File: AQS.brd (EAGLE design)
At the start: 70 x 60 mm, 44 parts, among them IC1 BME680, IC3 CP2102N-A01-GQFN24, IC4 ESPWROOM32, J1 ESP-PROG-2X3-1.27-SHROUDED, J2 M02X5-1.27-S, J3 USB-C-16P-16P, Q1 MMDT3904, Q2 2N7002

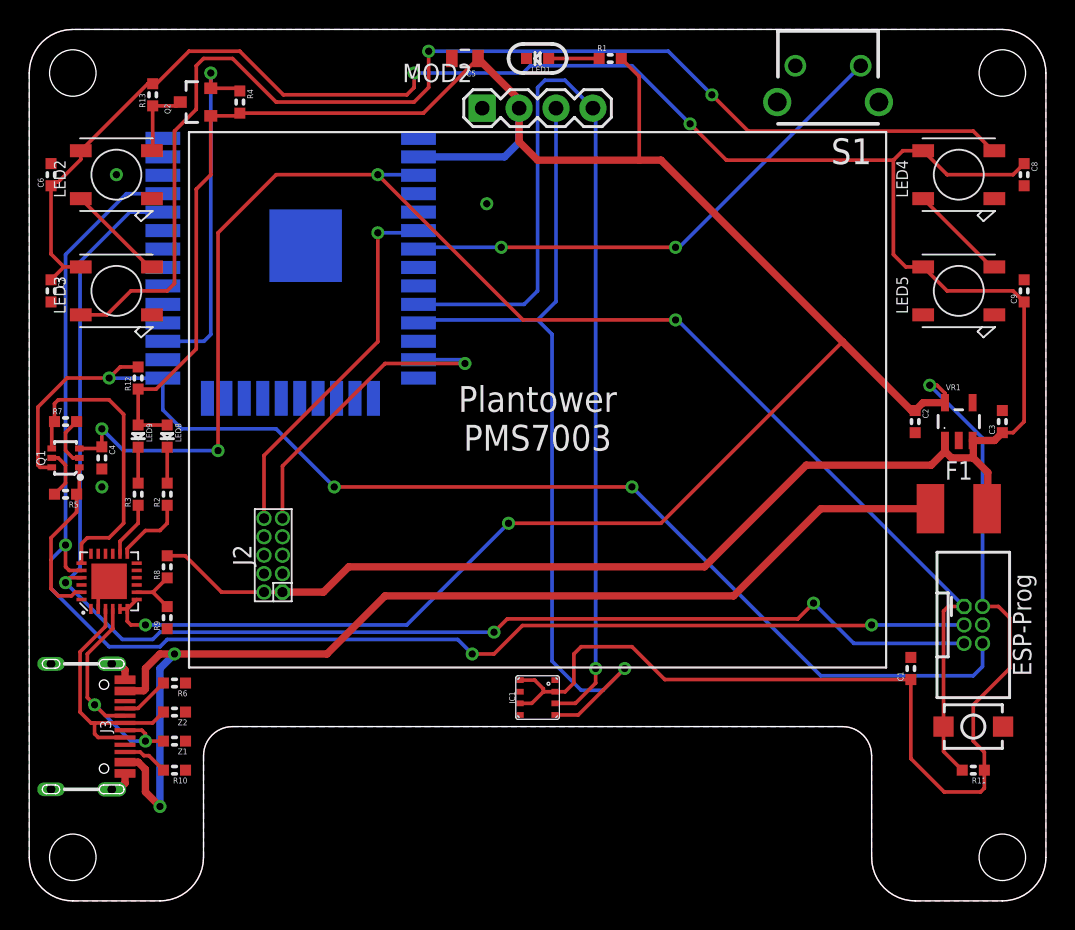
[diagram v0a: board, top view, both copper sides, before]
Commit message: Major update to use 240x240 SPI LCD
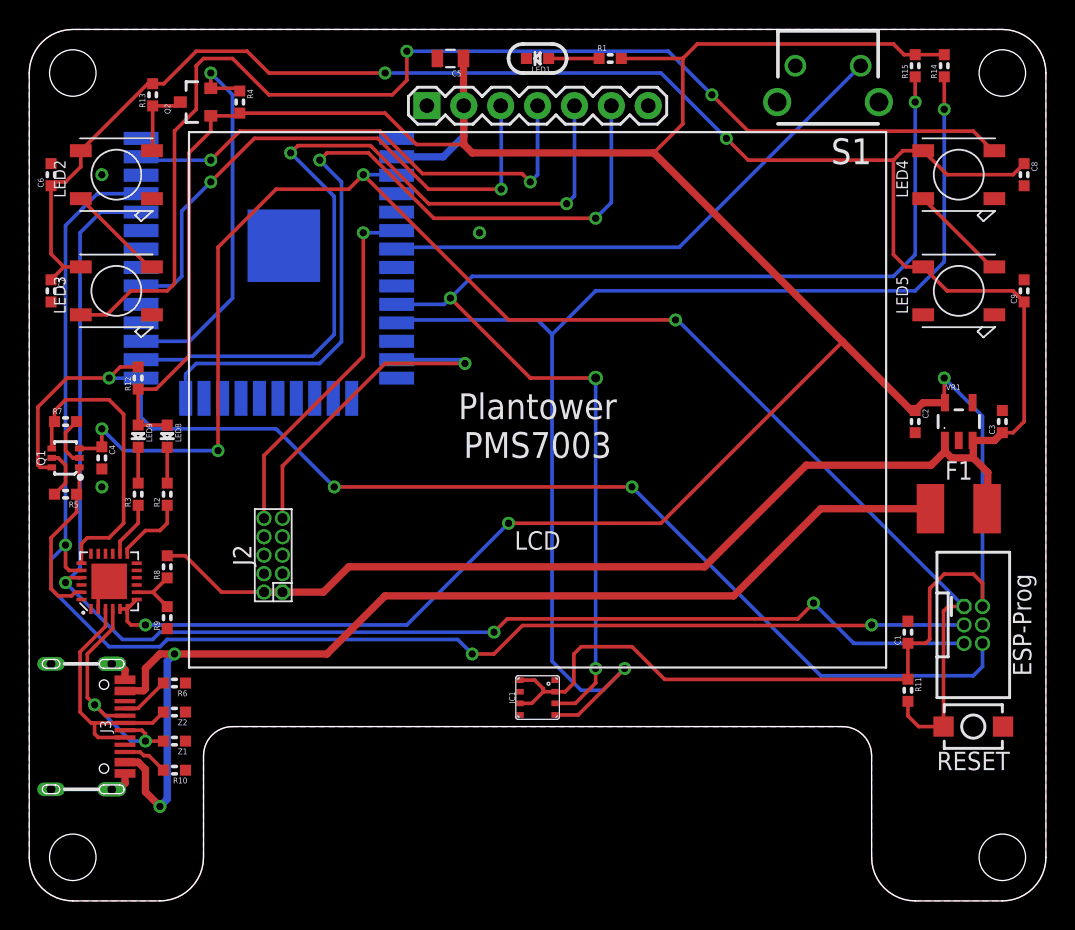
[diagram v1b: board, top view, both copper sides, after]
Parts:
- removed MOD2: OLED-I2C-128X64-0.96-HEADER, SuperHouse-Displays:OLED-128X64-0.96-HEADER
- added LCD: OLED-SPI-HEADER, SuperHouse-Displays:OLED-240X240-1.3-HEADER
- added R14, R15: 4K7, SuperHouse-DiscreteSemi:R0603
- moved R11 7.11 mm to (60.5, 15.5), turned to 270 degrees
- moved C1 2.51 mm to (60.5, 19.5)
- moved IC4 1.50 mm to (16.5, 55.0)
- moved C5 1.00 mm to (29.0, 59.0)
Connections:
- new net GPIO15: IC4.23
- new net GPIO18: IC4.30, LCD.SCK
- new net GPIO19: IC4.31
- new net GPIO2: IC4.24, LCD.DC
- new net GPIO23: IC4.37, LCD.SDA
- new net GPIO4: IC4.26, LCD.RES
- net 3.3V: now also LCD.VCC, R14.2, R15.2; no longer MOD2.VCC
- net GND: now also LCD.GND; no longer MOD2.GND
- net SCL: now also R14.1; no longer MOD2.SCL
- net SDA: now also R15.1; no longer MOD2.SDA
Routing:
- net GPIO2: track 0.00 -> 55.7 mm, vias 0 -> 2
- net GPIO4: track 0.00 -> 55.6 mm, vias 0 -> 2
- net GPIO18: track 0.00 -> 38.9 mm, vias 0 -> 2
- net GPIO23: track 0.00 -> 34.6 mm, vias 0 -> 2
- net SCL: track 59.9 -> 88.1 mm, vias 1 -> 2
- net SDA: track 70.4 -> 86.0 mm, vias 1 -> 4
- net 3.3V: track 246.6 -> 253.1 mm
- net GPIO16: track 24.6 -> 26.8 mm
- net 5V: track 182.0 -> 180.0 mm
- net PMS_SET: track 22.4 -> 23.9 mm
- net BUTTON: track 35.7 -> 37.2 mm, vias 2 -> 0
- net PMS_TX: track 25.8 -> 24.9 mm
- net !RESET: track 107.6 -> 106.8 mm
- net N$12: track 85.1 -> 84.4 mm
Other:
- board text added: "I2C Address: 0x77: BME680"
- board text added: "Pin Assignments: GPIO2: TFT_DC GPIO4: TFT_RST GPIO14: SET for PMS7003 GPIO15: TFT_CS GPIO16: WS2812B GPIO18: TFT_SCLK GPIO19: TFT_MISO GPIO23: TFT_MOSI GPIO25: SDA GPIO26: SCL GPIO34: Rx from PMS7003 Tx GPIO35: Button"
- board text added: "RESET"
- board text removed: "Pin Assignments: IO14: SET for PMS7003 IO16: WS2812B IO25: SDA IO26: SCL IO34: Rx from PMS7003 IO35: Button I2C Addresses: 0x3C: 128x64 OLED 0x77: BME280"

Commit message: Moved mode button to GPIO0
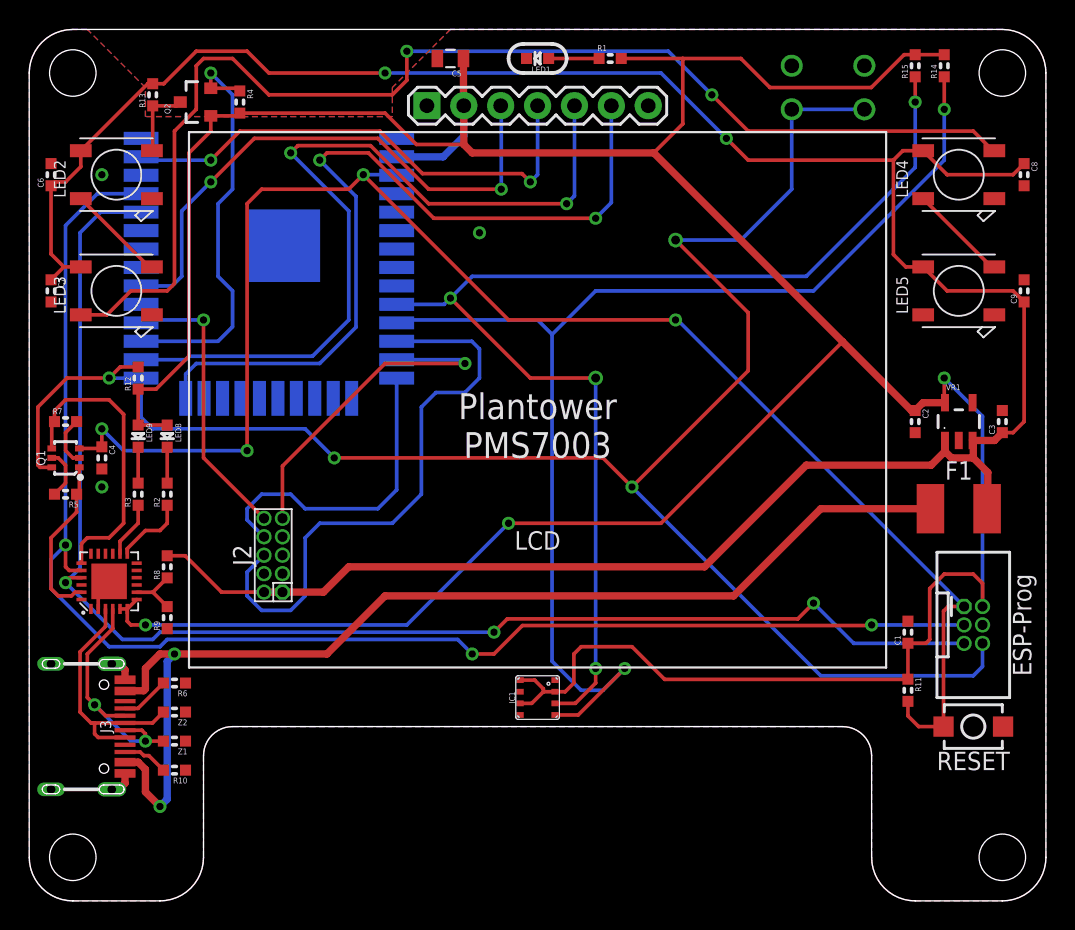
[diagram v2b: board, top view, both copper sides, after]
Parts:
- removed S1: TAC-SWITCH-2PIN-GND-FSMRAJ, SuperHouse-Switches:TYCO-FSMRAJ
- added S3: (no value), SuperHouse-Switches:TACTILE-PTH-4.5MM
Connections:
- removed net BUTTON: IC4.7, S1.1
- net GND: now also S3.3, S3.4; no longer S1.2, S1.TAB1, S1.TAB2
- net GPIO0: now also S3.1, S3.2
- net PMS_RESET: now also IC4.12
- net PMS_RX: now also IC4.14
- net PMS_TX: now also IC4.28; no longer IC4.6
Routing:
- net GPIO0: track 85.1 -> 127.5 mm, vias 3 -> 4
- net PMS_RESET: track 0.00 -> 40.1 mm
- net BUTTON: track 37.2 -> 0.00 mm
- net PMS_RX: track 0.00 -> 21.8 mm
- net PMS_TX: track 24.9 -> 19.8 mm
- net SCL: track 88.1 -> 84.0 mm
- net SDA: track 86.0 -> 82.5 mm
- net GPIO16: track 26.8 -> 28.8 mm
- net !RESET: track 106.8 -> 108.5 mm
- net 3.3V: track 253.1 -> 254.2 mm
- net GPIO4: track 55.6 -> 56.4 mm
- net GPIO2: track 55.7 -> 56.5 mm

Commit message: Replaced CP2102N with CH340G; removed 2 LEDs; reworked routing; moved button
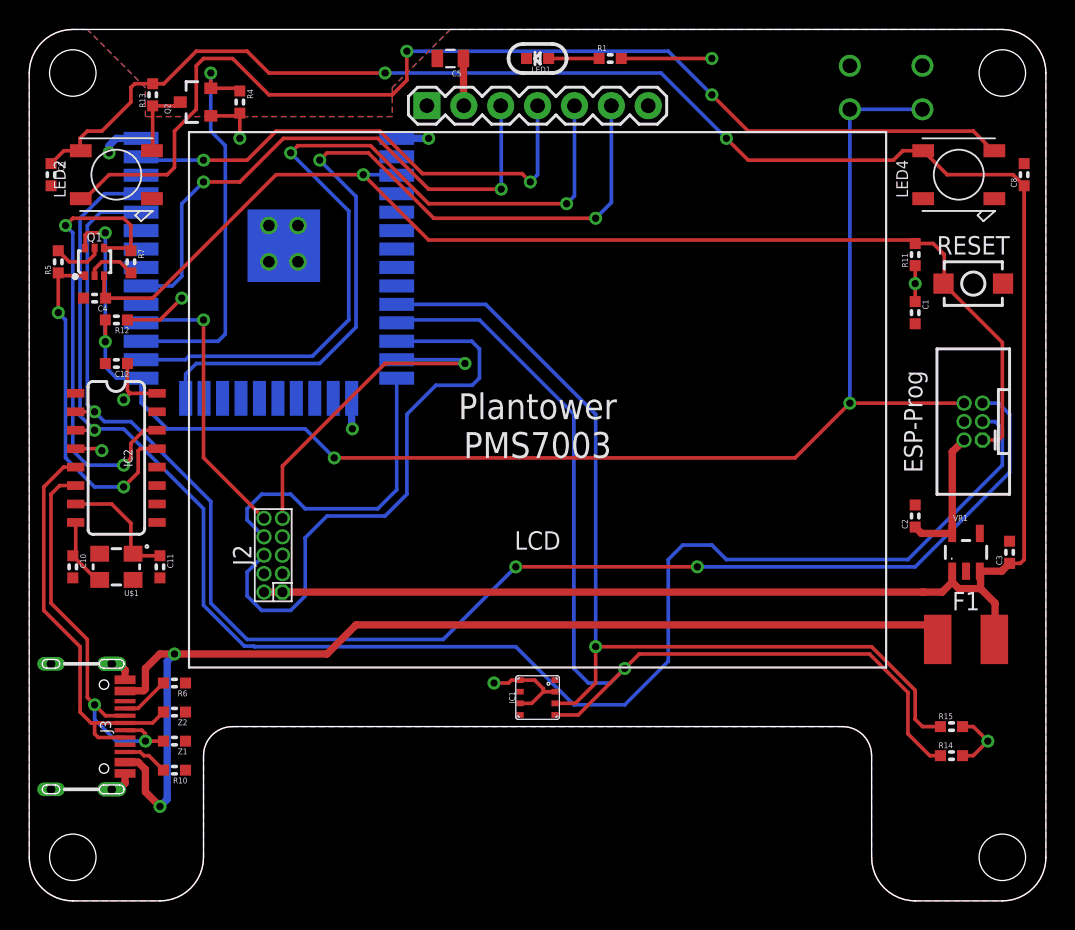
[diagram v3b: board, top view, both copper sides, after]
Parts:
- removed C7, C9: 100nF, SuperHouse-DiscreteSemi:C0603
- removed IC3: CP2102N-A01-GQFN24, SuperHouse-ICs:QFN-24
- removed LED3, LED5: WS2812B5050, SuperHouse-LEDs:WS2812B
- removed LED8: GREEN, SuperHouse-LEDs:LED-0603
- removed LED9: YELLOW, SuperHouse-LEDs:LED-0603
- removed R2, R3: 1K, SuperHouse-DiscreteSemi:R0603
- removed R8: 22.1K, SuperHouse-DiscreteSemi:R0603
- removed R9: 47.5K, SuperHouse-DiscreteSemi:R0603
- removed S3: (no value), SuperHouse-Switches:TACTILE-PTH-4.5MM
- added C10, C11: 22pF, SuperHouse-DiscreteSemi:C0603
- added C12: 100nF, SuperHouse-DiscreteSemi:C0603
- added IC2: CH340G, SuperHouse-ICs:SO16
- added S1: MODE, SuperHouse-Switches:TACTILE-PTH-4.5MM
- added U$1: 16MHz, SuperHouse-Oscillators:CRYSTAL-SMD-3X2
- C2: value 4.7uF -> 10uF
- C3: value 1uF -> 10uF
- moved R14 47.5 mm to (63.5, 11.0), turned to 0 degrees
- moved R15 45.6 mm to (63.5, 13.0), turned to 0 degrees
- moved S2 30.5 mm to (65.0, 43.5)
- moved R11 30.0 mm to (61.0, 45.5), turned to 90 degrees
- moved C1 22.0 mm to (61.0, 41.5), turned to 270 degrees
- moved R5 16.0 mm to (2.00, 45.0), turned to 90 degrees
- moved J1 14.0 mm to (65.0, 34.0), turned to 90 degrees
- moved Q1 13.6 mm to (4.50, 45.0), turned to 0 degrees
- moved R7 11.9 mm to (7.00, 45.0), turned to 270 degrees
- moved C4 11.0 mm to (4.50, 42.5), turned to 180 degrees
- moved C3 9.01 mm to (67.5, 25.0)
- moved F1 9.01 mm to (64.5, 19.0)
- moved VR1 9.01 mm to (64.5, 25.0)
- moved C2 6.50 mm to (61.0, 27.5), turned to 90 degrees
- moved R12 4.27 mm to (6.00, 41.0), turned to 180 degrees
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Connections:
- removed net ESP_RX: IC3.21, IC4.34, J1.5
- removed net ESP_TX: IC3.20, IC4.35, J1.3
- removed net GPIO15: IC4.23
- removed net GPIO19: IC4.31
- removed net N$13: LED4.2-DOUT, LED5.4-DIN
- removed net N$5: LED9.C, R3.2
- removed net N$6: IC3.8, R8.1, R9.2
- removed net N$9: LED2.2-DOUT, LED3.4-DIN
- new net RXD0: IC2.2, IC4.34, J1.5
- new net TXD0: IC2.3, IC4.35, J1.3
- net 3.3V: now also C12.1, IC2.16, IC2.4; no longer IC3.5, IC3.6, IC3.7, LED8.A, LED9.A
- net 5V: no longer C7.1, C9.1, LED3.1-VDD, LED5.1-VDD, R8.2
- net D+: now also IC2.5; no longer IC3.3
- net D-: now also IC2.6; no longer IC3.4
- net DTR: now also IC2.13; no longer IC3.23
- net GND: now also C10.2, C11.2, C12.2, IC2.1, S1.3, S1.4, U$1.2, U$1.4; no longer C7.2, C9.2, IC3.2, IC3.TGND, LED3.3-GND, LED5.3-GND, R9.1, S3.3, S3.4
- net GPIO0: now also S1.1, S1.2; no longer S3.1, S3.2
- net N$12: now also LED2.2-DOUT; no longer LED3.2-DOUT
- net N$2: now also C10.1, IC2.8, U$1.3; no longer IC3.14, R3.1
- net N$3: now also C11.1, IC2.7, U$1.1; no longer IC3.13, R2.1
- net N$4: now also IC4.6; no longer LED8.C, R2.2
- net RTS: now also IC2.14; no longer IC3.19
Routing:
- net 3.3V: track 254.2 -> 47.1 mm, vias 3 -> 8
- net TXD0: track 0.00 -> 111.3 mm, vias 0 -> 1
- net RXD0: track 0.00 -> 103.0 mm, vias 0 -> 3
- net ESP_TX: track 100.2 -> 0.00 mm, vias 3 -> 0
- net ESP_RX: track 96.3 -> 0.00 mm, vias 3 -> 0
- net !RESET: track 108.5 -> 83.1 mm, vias 4 -> 1
- net GPIO0: track 127.5 -> 102.6 mm
- net 5V: track 180.0 -> 160.6 mm
- net SDA: track 82.5 -> 65.9 mm, vias 4 -> 1
- net SCL: track 84.0 -> 69.7 mm, vias 2 -> 1
- net DTR: track 11.6 -> 23.9 mm, vias 0 -> 2
- net RTS: track 20.5 -> 32.1 mm, vias 0 -> 2
- net D+: track 17.1 -> 28.6 mm
- net D-: track 17.7 -> 28.5 mm
- net GND: track 5.74 -> 13.8 mm, vias 3 -> 7
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- added copper zone on layer 16, net 3.3V
- removed copper zone on layer 16, net GND
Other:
- board text added: "Pin Assignments: GPIO0: Button GPIO2: TFT_DC GPIO4: TFT_RST GPIO12: Tx to PMS7003 Rx GPIO14: PMS7003 SET GPIO15: TFT_CS GPIO16: WS2812B GPIO17: Rx from PMS7003 Tx GPIO18: TFT_SCLK GPIO19: TFT_MISO GPIO23: TFT_MOSI GPIO25: SDA GPIO26: SCL GPIO27: PMS7003 RESET"
- board text added: "v2.0"
- board text removed: "Pin Assignments: GPIO2: TFT_DC GPIO4: TFT_RST GPIO14: SET for PMS7003 GPIO15: TFT_CS GPIO16: WS2812B GPIO18: TFT_SCLK GPIO19: TFT_MISO GPIO23: TFT_MOSI GPIO25: SDA GPIO26: SCL GPIO34: Rx from PMS7003 Tx GPIO35: Button"
- board text removed: "v1.0"

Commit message: Replaced programming header
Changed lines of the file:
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@@
 <?xml version="1.0" encoding="utf-8"?>
 <!DOCTYPE eagle SYSTEM "eagle.dtd">
-<eagle version="9.6.0">
+<eagle version="9.6.2">
 <drawing>
 <settings>
@@
 </layers>
 <board>
-<fusionsync huburn="a.cGVyc29uYWw6dWUyZDliZmNi" projecturn="a.cGVyc29uYWw6dWUyZDliZmNiIzIwMjAwMjA0MjYyMzE5MjU2" f3durn="urn:adsk.wipprod:dm.lineage:aiuPCscQSwuDSL48b4mNzA" pcbguid="1fa1250c-e1c7-44ac-bd16-9546b0c881a2" lastpulledtime="" lastsyncedchangeguid="df6bc671-9ef7-6506-d196-8edb4a68a568" latestrevisionid="" lastsyncedrevisionid="" lastboardhashguid="" lastpushedtime="" linktopcb3d="%12"/>
+<fusionsync huburn="a.cGVyc29uYWw6dWUyZDliZmNi" projecturn="a.cGVyc29uYWw6dWUyZDliZmNiIzIwMjAwMjA0MjYyMzE5MjU2" f3durn="urn:adsk.wipprod:dm.lineage:aiuPCscQSwuDSL48b4mNzA" pcbguid="1fa1250c-e1c7-44ac-bd16-9546b0c881a2" lastpulledtime="" lastsyncedchangeguid="df6bc671-9ef7-6506-d196-8edb4a68a568" latestrevisionid="" lastsyncedrevisionid="" lastboardhashguid="" lastpushedtime="" linktopcb3d="false"/>
 <plain>
 <wire x1="70" y1="58" x2="70" y2="4" width="0.0254" layer="20"/>
@@
 <attribute name="VALUE" x="7.684" y="57.9348" size="0.8128" layer="27" font="vector"/>
 </element>
-<element name="J1" library="SuperHouse-ESP-Prog" library_urn="urn:adsk.eagle:library:14353672" package="2X3-1.27-SHROUDED" package3d_urn="urn:adsk.eagle:package:14377920/2" value="ESP-PROG-2X3-1.27-SHROUDED" x="65" y="34" smashed="yes" rot="R90">
+<element name="J1" library="SuperHouse-ESP-Prog" library_urn="urn:adsk.eagle:library:14353672" package="2X3-1.27-SHROUDED" package3d_urn="urn:adsk.eagle:package:14377920/3" value="ESP-PROG-2X3-1.27-SHROUDED" x="65" y="34" smashed="yes" rot="R90">
 <attribute name="NAME" x="62.3" y="34" size="1.27" layer="104" font="vector" rot="R270" align="top-center"/>
 </element>
@@
 <wire x1="61" y1="44.738" x2="61" y2="43.5" width="0.254" layer="1"/>
 <wire x1="63.55" y1="26.3001" x2="63.55" y2="31.915" width="0.508" layer="1"/>
-<wire x1="63.55" y1="31.915" x2="64.365" y2="32.73" width="0.508" layer="1"/>
 <wire x1="61.4379" y1="26.3001" x2="61" y2="26.738" width="0.508" layer="1"/>
 <wire x1="63.55" y1="26.3001" x2="61.4379" y2="26.3001" width="0.508" layer="1"/>
@@
 <wire x1="6.762" y1="41" x2="9" y2="41" width="0.254" layer="1"/>
 <wire x1="9" y1="41" x2="10.5" y2="42.5" width="0.254" layer="1"/>
+<wire x1="63.55" y1="31.915" x2="64.365" y2="32.73" width="0.508" layer="1"/>
 </signal>
 <signal name="N$1">
@@
 <wire x1="5.238" y1="47" x2="5.238" y2="39.5" width="0.254" layer="16"/>
 <wire x1="56.5" y1="55.5" x2="56.5" y2="35.27" width="0.254" layer="16"/>
-<wire x1="64.365" y1="35.27" x2="56.5" y2="35.27" width="0.254" layer="1"/>
 <wire x1="52.73" y1="31.5" x2="56.5" y2="35.27" width="0.254" layer="1"/>
 <wire x1="21" y1="31.5" x2="52.73" y2="31.5" width="0.254" layer="1"/>
+<wire x1="56.5" y1="35.27" x2="64.365" y2="35.27" width="0.254" layer="16"/>
 </signal>
 <signal name="N$7">
@@
 <wire x1="7.7" y1="49.69" x2="5.19" y2="49.69" width="0.254" layer="16"/>
 <contactref element="IC2" pad="3"/>
-<wire x1="65.635" y1="34" x2="66.5" y2="34" width="0.254" layer="16"/>
-<wire x1="66.5" y1="34" x2="67" y2="33.5" width="0.254" layer="16"/>
+<wire x1="67" y1="33.5" x2="66.5" y2="34" width="0.254" layer="16"/>
 <wire x1="67" y1="33.5" x2="67" y2="31" width="0.254" layer="16"/>
 <wire x1="67" y1="31" x2="60.5" y2="24.5" width="0.254" layer="16"/>
@@
 <wire x1="47" y1="25.5" x2="45" y2="25.5" width="0.254" layer="16"/>
 <wire x1="45" y1="25.5" x2="44" y2="24.5" width="0.254" layer="16"/>
+<wire x1="66.5" y1="34" x2="65.635" y2="34" width="0.254" layer="16"/>
 </signal>
 <signal name="RXD0">
@@
 <wire x1="7.7" y1="48.42" x2="4.92" y2="48.42" width="0.254" layer="16"/>
 <contactref element="IC2" pad="2"/>
-<wire x1="65.635" y1="35.27" x2="66.73" y2="35.27" width="0.254" layer="16"/>
-<wire x1="66.73" y1="35.27" x2="67.5" y2="34.5" width="0.254" layer="16"/>
+<wire x1="67.5" y1="34.5" x2="66.73" y2="35.27" width="0.254" layer="16"/>
 <wire x1="61" y1="24" x2="67.5" y2="30.5" width="0.254" layer="16"/>
 <wire x1="67.5" y1="34.5" x2="67.5" y2="30.5" width="0.254" layer="16"/>
@@
 <via x="46" y="24" extent="1-16" drill="0.5"/>
 <wire x1="46" y1="24" x2="61" y2="24" width="0.254" layer="16"/>
+<wire x1="66.73" y1="35.27" x2="65.635" y2="35.27" width="0.254" layer="16"/>
 </signal>
 <signal name="!RESET">
@@
 <wire x1="25.26" y1="51" x2="25.3" y2="50.96" width="0.254" layer="16"/>
 <wire x1="23" y1="51" x2="27.5" y2="46.5" width="0.254" layer="1"/>
-<wire x1="65.635" y1="32.73" x2="66.73" y2="32.73" width="0.254" layer="1"/>
-<wire x1="66.73" y1="32.73" x2="67" y2="33" width="0.254" layer="1"/>
+<wire x1="67" y1="33" x2="66.73" y2="32.73" width="0.254" layer="1"/>
 <wire x1="67" y1="39.45" x2="62.95" y2="43.5" width="0.254" layer="1"/>
 <wire x1="67" y1="33" x2="67" y2="39.45" width="0.254" layer="1"/>
@@
 <wire x1="8.5" y1="42.5" x2="5.262" y2="42.5" width="0.254" layer="1"/>
 <wire x1="17" y1="51" x2="8.5" y2="42.5" width="0.254" layer="1"/>
+<wire x1="66.73" y1="32.73" x2="65.635" y2="32.73" width="0.254" layer="1"/>
 </signal>
 <signal name="PMS_SET">
